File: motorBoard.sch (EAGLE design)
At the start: 8 parts, among them IC1 PIC18F4550_TQFP

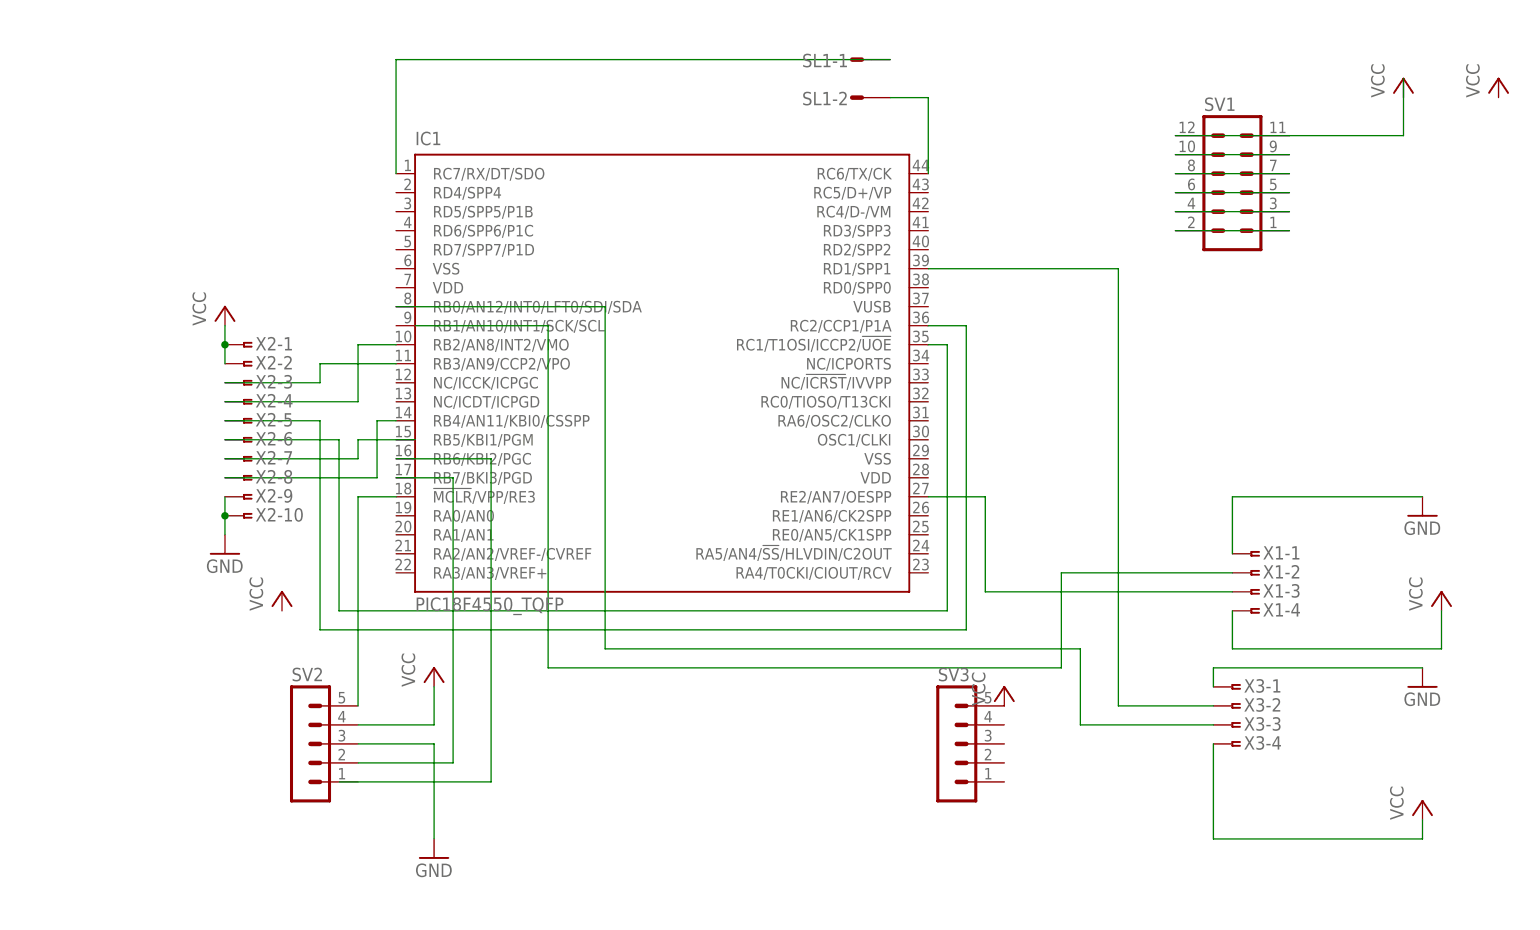
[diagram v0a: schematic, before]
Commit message: fixed schematic and replaced some connectors with micromatch
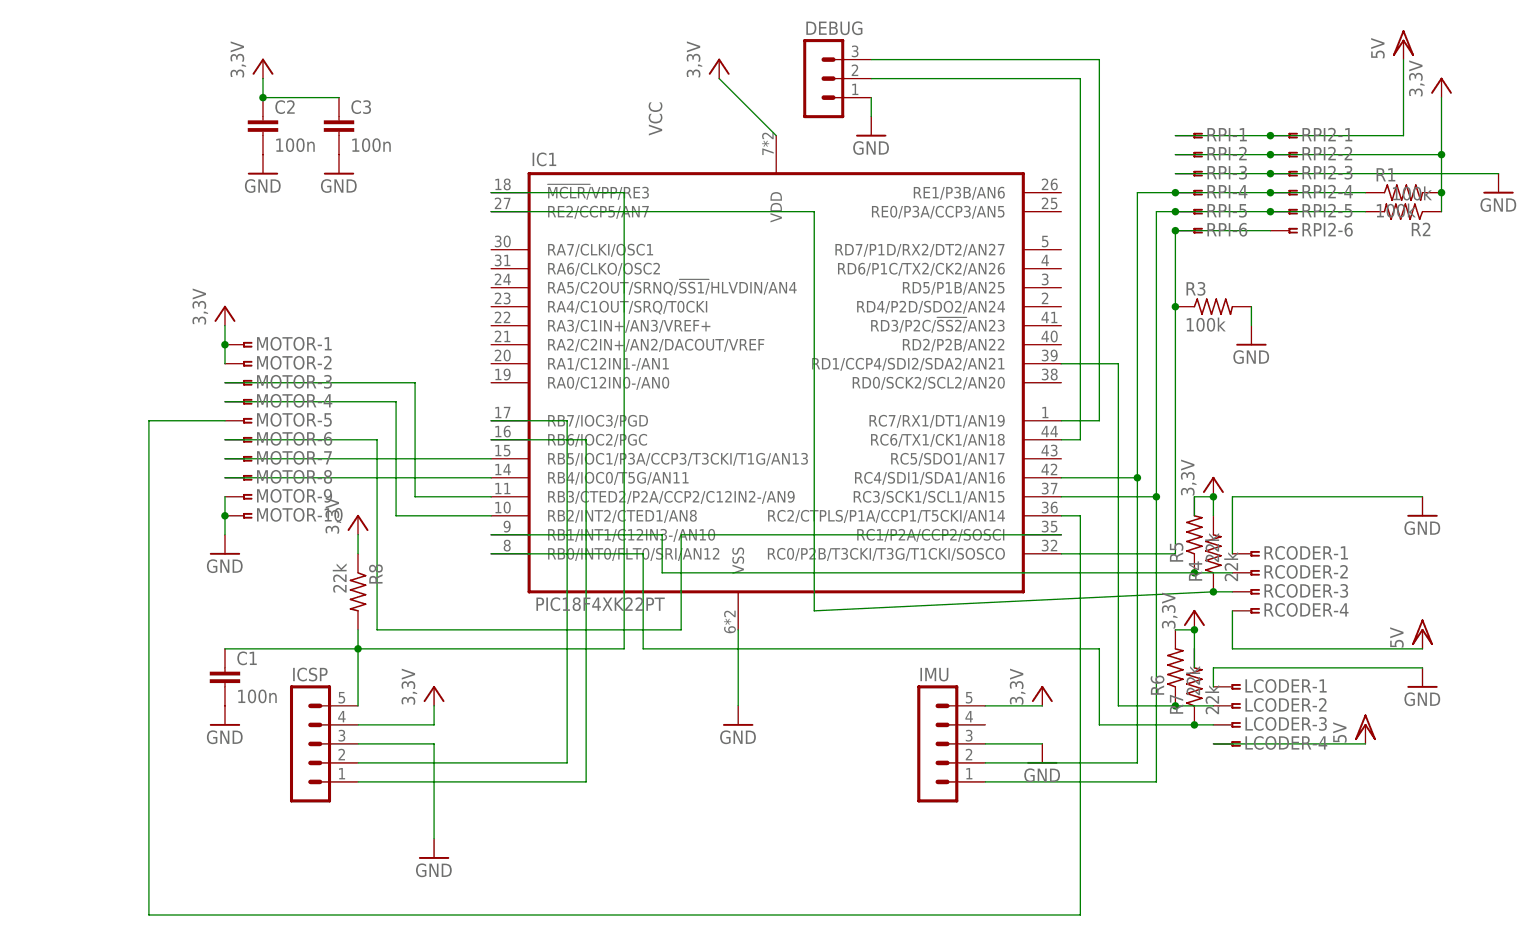
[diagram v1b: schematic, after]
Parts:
- removed SL1: (no value), con-amp-quick:MA02S
- removed SV1: (no value), con-lstb:MA06-2
- removed SV3: (no value), con-lstb:MA05-1
- added C1, C2, C3: 100n, resistor:C-EUC0805
- added DEBUG: (no value), con-lstb:MA03-1
- added IMU: (no value), con-lstb:MA05-1
- added R1, R2, R3: 100k, resistor:R-US_R0805
- added R4, R5, R6, R7: 22k, resistor:R-US_R0805
- added R8: 22k, resistor:R-US_M0805
- added RPI, RPI2: (no value), con-amp:SMDTOP-6
- IC1: value PIC18F4550_TQFP -> PIC18F4XK22PT; device microchip:PIC18F4550_TQFP -> microchip-pic18f4xk22:PIC18F4XK22PT
- renumbered SV2 to ICSP, X1 to RCODER, X2 to MOTOR, X3 to LCODER
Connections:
- removed net N$10: SV1.10, SV1.9
- removed net N$14: IC1.RC7/RX/DT/SDO, SL1-1.S
- removed net N$15: IC1.RC6/TX/CK, SL1-2.S
- removed net N$9: SV1.11, SV1.12
- new net N$23: IC1.RC2/CTPLS/P1A/CCP1/T5CKI/AN14, MOTOR-5.1
- new net N$8: IC1.RB5/IOC1/P3A/CCP3/T3CKI/T1G/AN13, MOTOR-7.1
- new net VDD: LCODER-4.1, RCODER-4.1, RPI-1.1, RPI2-1.1
- net GND: now also C1.2, C2.2, C3.2, DEBUG.1, IC1.VSS, IMU.3, R3.2, RPI-3.1, RPI2-3.1
- net N$1: now also IC1.RE2/CCP5/AN7, R4.1, RCODER-3.1; no longer IC1.RC1/T1OSI/ICCP2/!UOE, MOTOR-6.1
- net N$11: now also IC1.RD1/CCP4/SDI2/SDA2/AN21, R6.1; no longer IC1.RD1/SPP1
- net N$12: now also DEBUG.3, IC1.RC7/RX1/DT1/AN19; no longer IC1.RB0/AN12/INT0/LFT0/SDI/SDA, LCODER-3.1
- net N$13: now also IC1.RB1/INT1/C12IN3-/AN10, R5.1; no longer IC1.RE2/AN7/OESPP, RCODER-3.1
- net N$16: now also DEBUG.2, IC1.RC6/TX1/CK1/AN18; no longer IC1.!MCLR!/VPP/RE3, ICSP.5
- net N$17: now also IC1.RB7/IOC3/PGD; no longer IC1.RB7/BKI3/PGD
- net N$18: now also C1.1, IC1.!MCLR/!VPP/RE3, ICSP.5, R8.2; no longer SV1.7, SV1.8
- net N$19: now also IC1.RC4/SDI1/SDA1/AN16, IMU.2, R1.1, RPI-4.1, RPI2-4.1; no longer SV1.5, SV1.6
- net N$2: now also IC1.RB3/CTED2/P2A/CCP2/C12IN2-/AN9; no longer IC1.RB3/AN9/CCP2/VPO
- net N$20: now also IC1.RC3/SCK1/SCL1/AN15, IMU.1, R2.2, RPI-5.1, RPI2-5.1; no longer SV1.3, SV1.4
- net N$21: now also IC1.RC0/P2B/T3CKI/T3G/T1CKI/SOSCO, R3.1, RPI-6.1, RPI2-6.1; no longer SV1.1, SV1.2
- net N$3: now also IC1.RB2/INT2/CTED1/AN8; no longer IC1.RB2/AN8/INT2/VMO
- net N$4: now also IC1.RC1/P2A/CCP2/SOSCI, MOTOR-6.1; no longer IC1.RC2/CCP1/P1A, MOTOR-5.1
- net N$5: now also IC1.RB6/IOC2/PGC, ICSP.1; no longer IC1.RB6/KBI2/PGC
- net N$6: now also IC1.RB4/IOC0/T5G/AN11; no longer IC1.RB4/AN11/KBI0/CSSPP
- net N$7: now also IC1.RB0/INT0/FLT0/SRI/AN12, LCODER-3.1, R7.1; no longer MOTOR-7.1
- net VCC: now also C2.1, C3.1, IC1.VDD, IMU.5, R1.2, R2.1, R4.2, R5.2, R6.2, R7.2, R8.1, RPI-2.1, RPI2-2.1; no longer LCODER-4.1, RCODER-4.1, SV3.5

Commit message: board almost finished
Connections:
- net N$12: now also DEBUG.2; no longer DEBUG.3
- net N$16: now also DEBUG.3; no longer DEBUG.2
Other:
- moved on the sheet: R4
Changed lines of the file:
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@@
 <grid distance="0.1" unitdist="inch" unit="inch" style="lines" multiple="1" display="no" altdistance="0.01" altunitdist="inch" altunit="inch"/>
 <layers>
-<layer number="1" name="Top" color="4" fill="1" visible="yes" active="no"/>
-<layer number="16" name="Bottom" color="1" fill="1" visible="yes" active="no"/>
-<layer number="17" name="Pads" color="2" fill="1" visible="yes" active="no"/>
-<layer number="18" name="Vias" color="2" fill="1" visible="yes" active="no"/>
-<layer number="19" name="Unrouted" color="6" fill="1" visible="yes" active="no"/>
-<layer number="20" name="Dimension" color="15" fill="1" visible="yes" active="no"/>
-<layer number="21" name="tPlace" color="7" fill="1" visible="yes" active="no"/>
-<layer number="22" name="bPlace" color="7" fill="1" visible="yes" active="no"/>
-<layer number="23" name="tOrigins" color="15" fill="1" visible="yes" active="no"/>
-<layer number="24" name="bOrigins" color="15" fill="1" visible="yes" active="no"/>
-<layer number="25" name="tNames" color="7" fill="1" visible="yes" active="no"/>
-<layer number="26" name="bNames" color="7" fill="1" visible="yes" active="no"/>
-<layer number="27" name="tValues" color="7" fill="1" visible="yes" active="no"/>
-<layer number="28" name="bValues" color="7" fill="1" visible="yes" active="no"/>
+<layer number="1" name="Top" color="4" fill="1" visible="no" active="no"/>
+<layer number="16" name="Bottom" color="1" fill="1" visible="no" active="no"/>
+<layer number="17" name="Pads" color="2" fill="1" visible="no" active="no"/>
+<layer number="18" name="Vias" color="2" fill="1" visible="no" active="no"/>
+<layer number="19" name="Unrouted" color="6" fill="1" visible="no" active="no"/>
+<layer number="20" name="Dimension" color="15" fill="1" visible="no" active="no"/>
+<layer number="21" name="tPlace" color="7" fill="1" visible="no" active="no"/>
+<layer number="22" name="bPlace" color="7" fill="1" visible="no" active="no"/>
+<layer number="23" name="tOrigins" color="15" fill="1" visible="no" active="no"/>
+<layer number="24" name="bOrigins" color="15" fill="1" visible="no" active="no"/>
+<layer number="25" name="tNames" color="7" fill="1" visible="no" active="no"/>
+<layer number="26" name="bNames" color="7" fill="1" visible="no" active="no"/>
+<layer number="27" name="tValues" color="7" fill="1" visible="no" active="no"/>
+<layer number="28" name="bValues" color="7" fill="1" visible="no" active="no"/>
 <layer number="29" name="tStop" color="7" fill="3" visible="no" active="no"/>
 <layer number="30" name="bStop" color="7" fill="6" visible="no" active="no"/>
@@
 <layer number="35" name="tGlue" color="7" fill="4" visible="no" active="no"/>
 <layer number="36" name="bGlue" color="7" fill="5" visible="no" active="no"/>
-<layer number="37" name="tTest" color="7" fill="1" visible="yes" active="no"/>
-<layer number="38" name="bTest" color="7" fill="1" visible="yes" active="no"/>
+<layer number="37" name="tTest" color="7" fill="1" visible="no" active="no"/>
+<layer number="38" name="bTest" color="7" fill="1" visible="no" active="no"/>
 <layer number="39" name="tKeepout" color="4" fill="11" visible="no" active="no"/>
 <layer number="40" name="bKeepout" color="1" fill="11" visible="no" active="no"/>
@@
 <layer number="44" name="Drills" color="7" fill="1" visible="no" active="no"/>
 <layer number="45" name="Holes" color="7" fill="1" visible="no" active="no"/>
-<layer number="46" name="Milling" color="3" fill="1" visible="yes" active="no"/>
-<layer number="47" name="Measures" color="7" fill="1" visible="yes" active="no"/>
-<layer number="48" name="Document" color="7" fill="1" visible="yes" active="no"/>
-<layer number="49" name="Reference" color="7" fill="1" visible="yes" active="no"/>
-<layer number="51" name="tDocu" color="7" fill="1" visible="yes" active="no"/>
-<layer number="52" name="bDocu" color="7" fill="1" visible="yes" active="no"/>
+<layer number="46" name="Milling" color="3" fill="1" visible="no" active="no"/>
+<layer number="47" name="Measures" color="7" fill="1" visible="no" active="no"/>
+<layer number="48" name="Document" color="7" fill="1" visible="no" active="no"/>
+<layer number="49" name="Reference" color="7" fill="1" visible="no" active="no"/>
+<layer number="51" name="tDocu" color="7" fill="1" visible="no" active="no"/>
+<layer number="52" name="bDocu" color="7" fill="1" visible="no" active="no"/>
 <layer number="90" name="Modules" color="5" fill="1" visible="yes" active="yes"/>
 <layer number="91" name="Nets" color="2" fill="1" visible="yes" active="yes"/>
@@
 <instance part="IC1" gate="G$1" x="50.8" y="55.88"/>
 <instance part="GND5" gate="1" x="147.32" y="81.28"/>
-<instance part="GND6" gate="1" x="86.36" y="5.08"/>
+<instance part="GND6" gate="1" x="86.36" y="7.62" rot="R90"/>
 <instance part="R1" gate="G$1" x="134.62" y="81.28"/>
 <instance part="R2" gate="G$1" x="134.62" y="78.74" rot="R180"/>
 <instance part="R3" gate="G$1" x="109.22" y="66.04"/>
-<instance part="R4" gate="G$1" x="109.22" y="33.02" rot="R90"/>
+<instance part="R4" gate="G$1" x="109.22" y="38.1" rot="R90"/>
 <instance part="R5" gate="G$1" x="106.68" y="35.56" rot="R90"/>
 <instance part="R6" gate="G$1" x="104.14" y="17.78" rot="R90"/>
 <instance part="R7" gate="G$1" x="106.68" y="15.24" rot="R90"/>
 <instance part="P+9" gate="VCC" x="106.68" y="25.4"/>
-<instance part="P+10" gate="VCC" x="109.22" y="43.18"/>
+<instance part="P+10" gate="VCC" x="106.68" y="45.72"/>
 <instance part="GND7" gate="1" x="114.3" y="60.96"/>
 <instance part="R8" gate="G$1" x="-5.08" y="27.94" rot="R270"/>
@@
 <instance part="VDD1" gate="G$1" x="134.62" y="101.6"/>
 <instance part="VDD2" gate="G$1" x="137.16" y="22.86"/>
-<instance part="VDD3" gate="G$1" x="129.54" y="10.16"/>
+<instance part="VDD3" gate="G$1" x="104.14" y="7.62" rot="R90"/>
 <instance part="P+2" gate="VCC" x="-17.78" y="99.06"/>
 <instance part="DEBUG" gate="G$1" x="55.88" y="96.52"/>
@@
 <wire x1="104.14" y1="22.86" x2="106.68" y2="22.86" width="0.1524" layer="91"/>
 <wire x1="106.68" y1="22.86" x2="106.68" y2="20.32" width="0.1524" layer="91"/>
-<wire x1="106.68" y1="20.32" x2="106.68" y2="17.78" width="0.1524" layer="91"/>
 <pinref part="P+9" gate="VCC" pin="VCC"/>
 <junction x="106.68" y="22.86"/>
 </segment>
 <segment>
+<wire x1="106.68" y1="43.18" x2="109.22" y2="43.18" width="0.1524" layer="91"/>
+<pinref part="P+10" gate="VCC" pin="VCC"/>
+<pinref part="R4" gate="G$1" pin="2"/>
 <pinref part="R5" gate="G$1" pin="2"/>
-<wire x1="106.68" y1="38.1" x2="106.68" y2="40.64" width="0.1524" layer="91"/>
-<wire x1="106.68" y1="40.64" x2="109.22" y2="40.64" width="0.1524" layer="91"/>
-<wire x1="109.22" y1="40.64" x2="109.22" y2="38.1" width="0.1524" layer="91"/>
-<pinref part="P+10" gate="VCC" pin="VCC"/>
-<junction x="109.22" y="40.64"/>
-<pinref part="R4" gate="G$1" pin="2"/>
+<wire x1="106.68" y1="40.64" x2="106.68" y2="43.18" width="0.1524" layer="91"/>
+<junction x="106.68" y="43.18"/>
 </segment>
 <segment>
@@
 </segment>
 <segment>
-<wire x1="78.74" y1="7.62" x2="86.36" y2="7.62" width="0.1524" layer="91"/>
+<wire x1="78.74" y1="7.62" x2="83.82" y2="7.62" width="0.1524" layer="91"/>
 <pinref part="IMU" gate="G$1" pin="3"/>
 <pinref part="GND6" gate="1" pin="GND"/>
@@
 <net name="N$1" class="0">
 <segment>
-<wire x1="109.22" y1="27.94" x2="55.88" y2="25.4" width="0.1524" layer="91"/>
+<wire x1="111.76" y1="27.94" x2="109.22" y2="27.94" width="0.1524" layer="91"/>
+<wire x1="109.22" y1="27.94" x2="104.14" y2="27.94" width="0.1524" layer="91"/>
+<wire x1="104.14" y1="27.94" x2="104.14" y2="25.4" width="0.1524" layer="91"/>
+<wire x1="104.14" y1="25.4" x2="55.88" y2="25.4" width="0.1524" layer="91"/>
 <wire x1="55.88" y1="25.4" x2="55.88" y2="78.74" width="0.1524" layer="91"/>
 <wire x1="55.88" y1="78.74" x2="12.7" y2="78.74" width="0.1524" layer="91"/>
-<pinref part="R4" gate="G$1" pin="1"/>
 <pinref part="IC1" gate="G$1" pin="RE2/CCP5/AN7"/>
 <pinref part="RCODER" gate="-3" pin="1"/>
-<wire x1="109.22" y1="27.94" x2="111.76" y2="27.94" width="0.1524" layer="91"/>
+<pinref part="R4" gate="G$1" pin="1"/>
+<wire x1="109.22" y1="33.02" x2="109.22" y2="27.94" width="0.1524" layer="91"/>
 <junction x="109.22" y="27.94"/>
 </segment>
@@
 <pinref part="IC1" gate="G$1" pin="RC6/TX1/CK1/AN18"/>
 <wire x1="88.9" y1="48.26" x2="91.44" y2="48.26" width="0.1524" layer="91"/>
-<wire x1="91.44" y1="48.26" x2="91.44" y2="96.52" width="0.1524" layer="91"/>
-<wire x1="91.44" y1="96.52" x2="63.5" y2="96.52" width="0.1524" layer="91"/>
-<pinref part="DEBUG" gate="G$1" pin="2"/>
+<wire x1="91.44" y1="48.26" x2="91.44" y2="99.06" width="0.1524" layer="91"/>
+<pinref part="DEBUG" gate="G$1" pin="3"/>
+<wire x1="91.44" y1="99.06" x2="63.5" y2="99.06" width="0.1524" layer="91"/>
 </segment>
 </net>
@@
 <segment>
 <wire x1="88.9" y1="50.8" x2="93.98" y2="50.8" width="0.1524" layer="91"/>
-<wire x1="93.98" y1="50.8" x2="93.98" y2="99.06" width="0.1524" layer="91"/>
-<wire x1="93.98" y1="99.06" x2="63.5" y2="99.06" width="0.1524" layer="91"/>
+<wire x1="93.98" y1="50.8" x2="93.98" y2="96.52" width="0.1524" layer="91"/>
 <pinref part="IC1" gate="G$1" pin="RC7/RX1/DT1/AN19"/>
-<pinref part="DEBUG" gate="G$1" pin="3"/>
+<pinref part="DEBUG" gate="G$1" pin="2"/>
+<wire x1="93.98" y1="96.52" x2="63.5" y2="96.52" width="0.1524" layer="91"/>
 </segment>
 </net>
@@
 <pinref part="LCODER" gate="-4" pin="1"/>
 <pinref part="VDD3" gate="G$1" pin="VDD"/>
-<wire x1="129.54" y1="7.62" x2="109.22" y2="7.62" width="0.1524" layer="91"/>
+<wire x1="106.68" y1="7.62" x2="109.22" y2="7.62" width="0.1524" layer="91"/>
 </segment>
 </net>
@@
 </sheet>
 </sheets>
+<errors>
+</errors>
 </schematic>
 </drawing>
